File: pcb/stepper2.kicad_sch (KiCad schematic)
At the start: 52 parts, among them J1 DA15_Receptacle_MountingHoles, J10 Conn_01x07_Pin, J11 FAN, J2 DA15_Receptacle_MountingHoles, J3 DA15_Receptacle_MountingHoles, J4 DE15_Receptacle_HighDensity, J5 DE15_Receptacle_HighDensity, J6 DE15_Receptacle_HighDensity, J7 Conn_01x04_Pin, J8 Conn_01x05_Pin, J9 Conn_01x06_Pin, SW1 SW_Push, U1 AM26LS32ACN, U2 AM26LS32Ax, U3 AM26LS32ACN, U4 TMC2209_BIGTREETECH, U5 TMC2209_BIGTREETECH, U6 TMC2209_BIGTREETECH

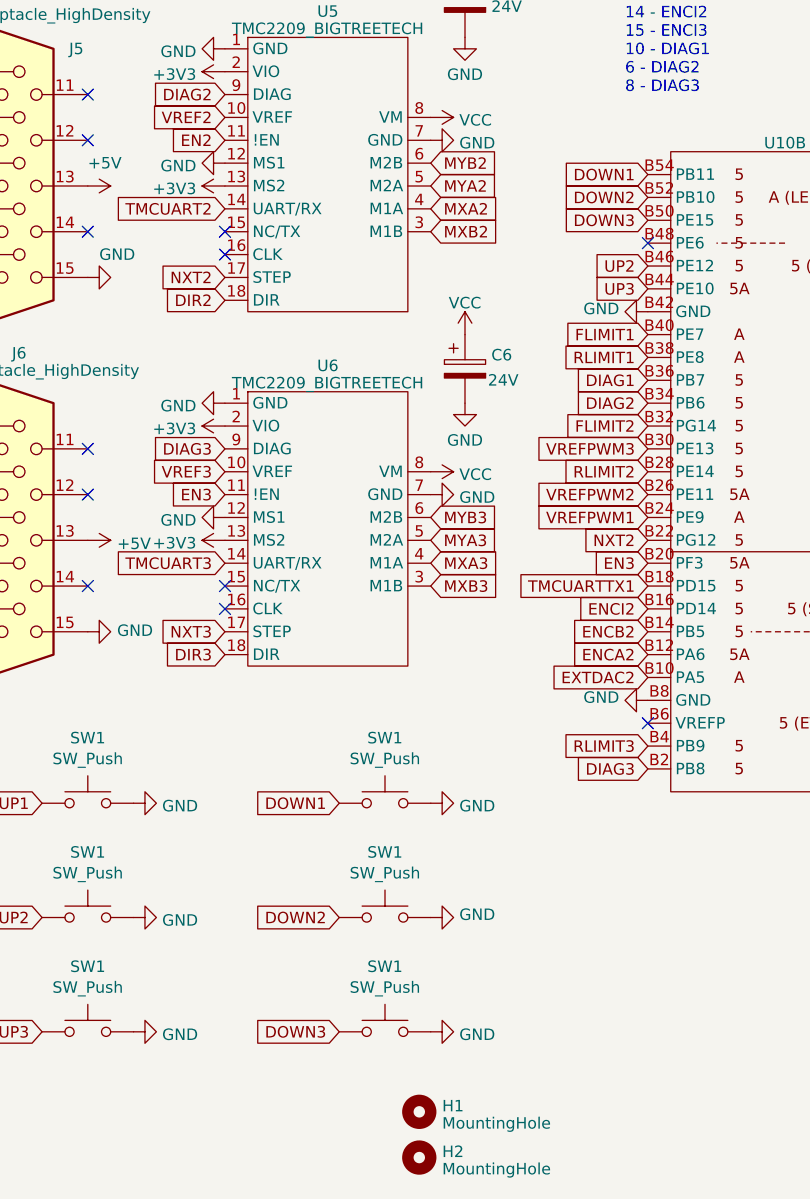
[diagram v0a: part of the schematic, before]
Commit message: fixed mixed labeling for jog buttons; initial config of the NXT timers
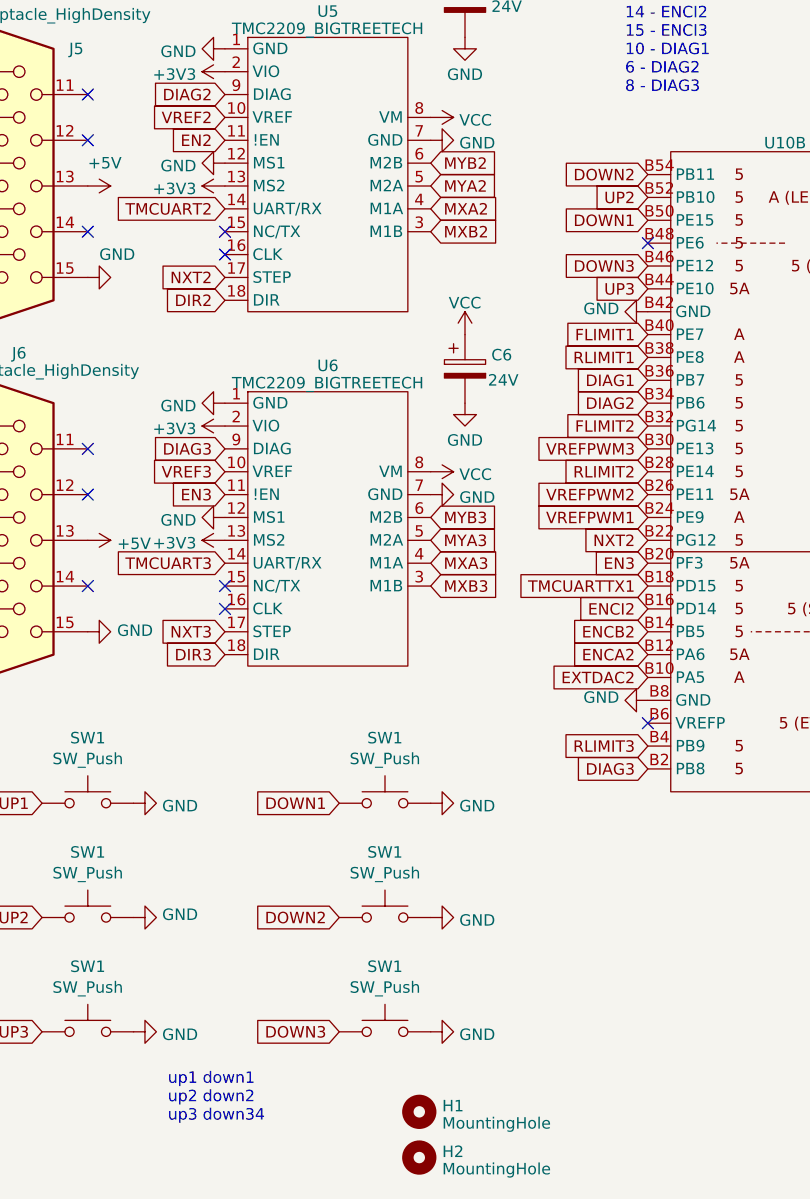
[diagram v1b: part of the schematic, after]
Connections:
- net DOWN1: now also SW1.1, U10.B50 (PE15); no longer SW1.1, U10.B54 (PB11)
- net DOWN2: now also SW1.1, U10.B54 (PB11); no longer SW1.1, U10.B52 (PB10)
- net DOWN3: now also SW1.1, U10.B46 (PE12); no longer SW1.1, U10.B50 (PE15)
- net UP2: now also SW1.1, U10.B52 (PB10); no longer SW1.1, U10.B46 (PE12)
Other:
- note added: "up1 down1 up2 down2 up3 down34"
- moved on the sheet: SW1

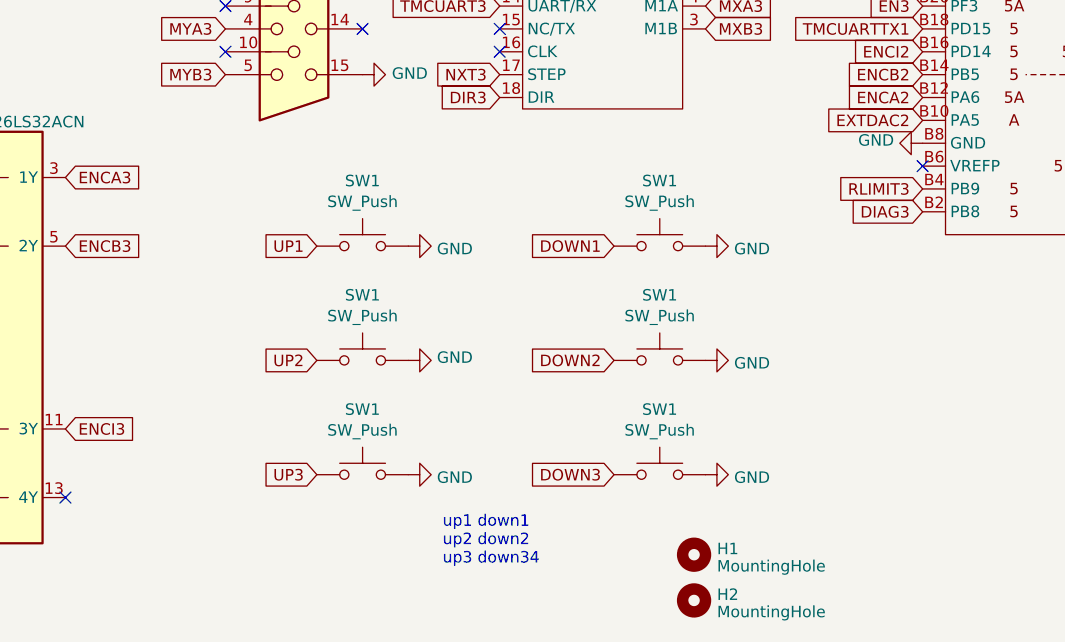
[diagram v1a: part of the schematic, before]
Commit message: PCB: NXT/DIR external output connectors and some polishing
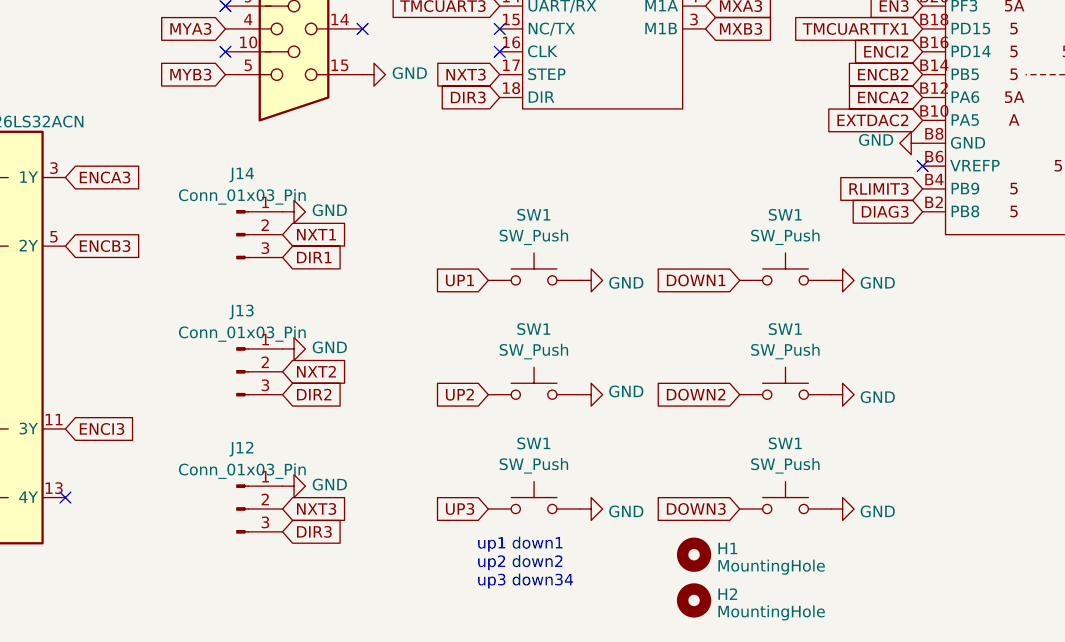
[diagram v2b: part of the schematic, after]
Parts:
- added J12, J13, J14: Conn_01x03_Pin, stepper2:JST_PH_S3B-PH-SM4-TB_1x03-1MP_P2.00mm_Horizontal, symbol Connector:Conn_01x03_Pin
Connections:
- net DIR1: now also J14.3 (Pin_3)
- net DIR2: now also J13.3 (Pin_3)
- net DIR3: now also J12.3 (Pin_3)
- net GND: now also J12.1 (Pin_1), J13.1 (Pin_1), J14.1 (Pin_1)
- net NXT1: now also J14.2 (Pin_2)
- net NXT2: now also J13.2 (Pin_2)
- net NXT3: now also J12.2 (Pin_2)
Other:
- moved on the sheet: SW1

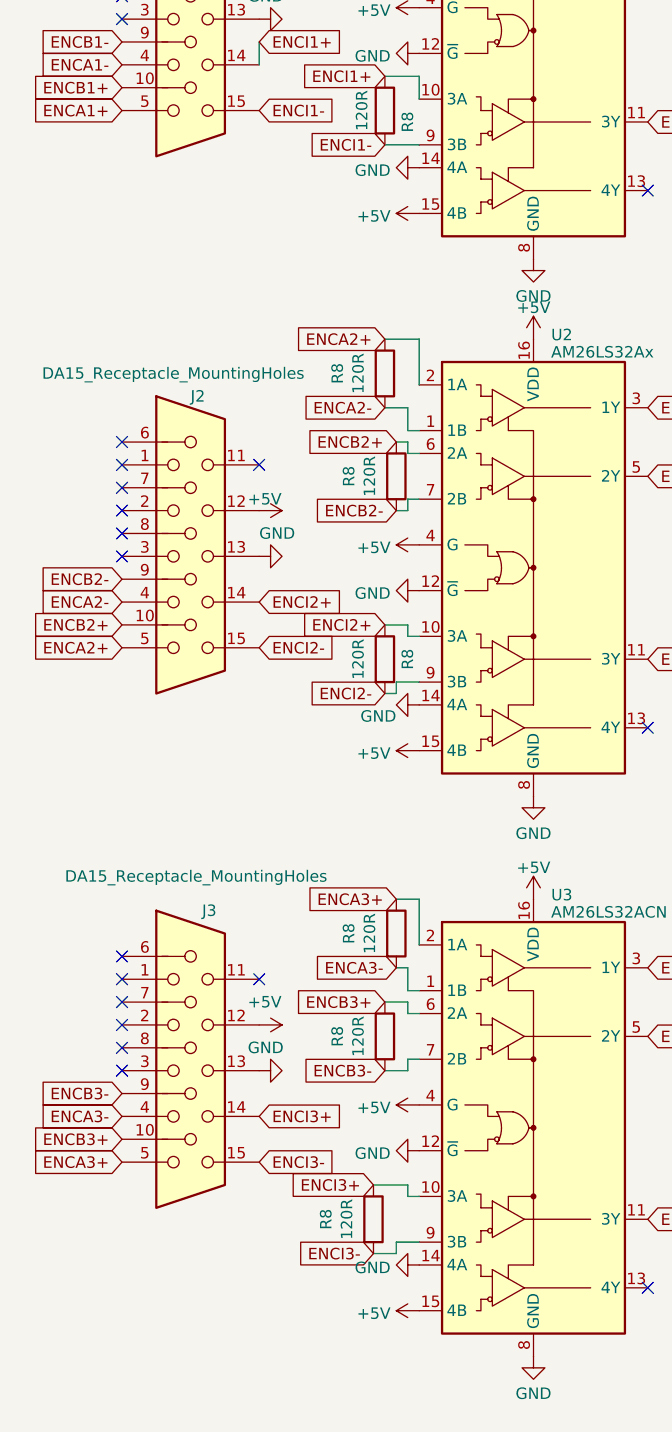
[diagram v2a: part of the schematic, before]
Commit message: filtering capacitors for differential receivers; BOM and placement files for SMD elements
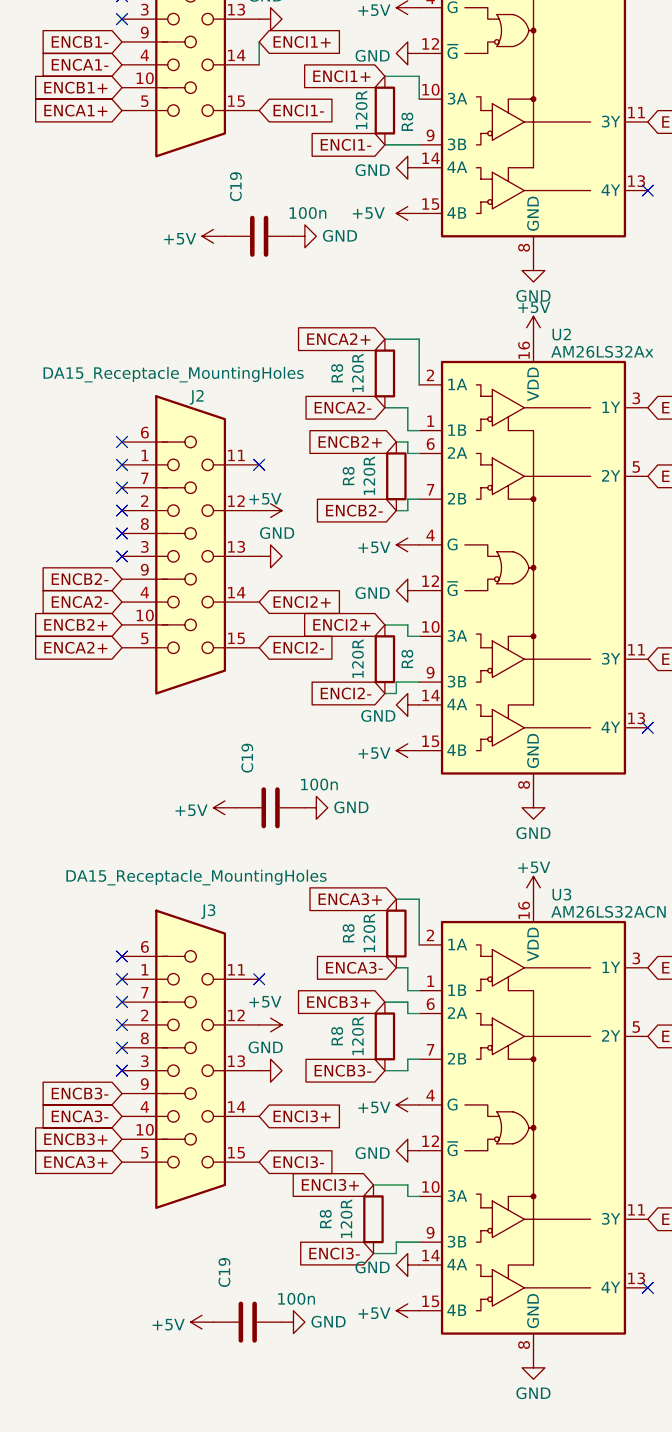
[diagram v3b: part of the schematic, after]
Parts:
- added C19 (x3): 100n, Capacitor_SMD:C_1206_3216Metric_Pad1.33x1.80mm_HandSolder, symbol Device:C
- C19: LCSC (none) -> C12891
- C4, C5, C6: LCSC (none) -> C2880403
- C7: LCSC (none) -> C310836
- J10: LCSC (none) -> C2856758
- J12, J13, J14: LCSC (none) -> C2688785
- J7: LCSC (none) -> C2688786
- J8: LCSC (none) -> C2874530
- J9: LCSC (none) -> C2874531
- R8: LCSC (none) -> C17909
- R8: LCSC (none) -> C17902
- R8: LCSC (none) -> C4410
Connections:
- net +5V: now also C19.1, C19.1, C19.1
- net GND: now also C19.2, C19.2, C19.2

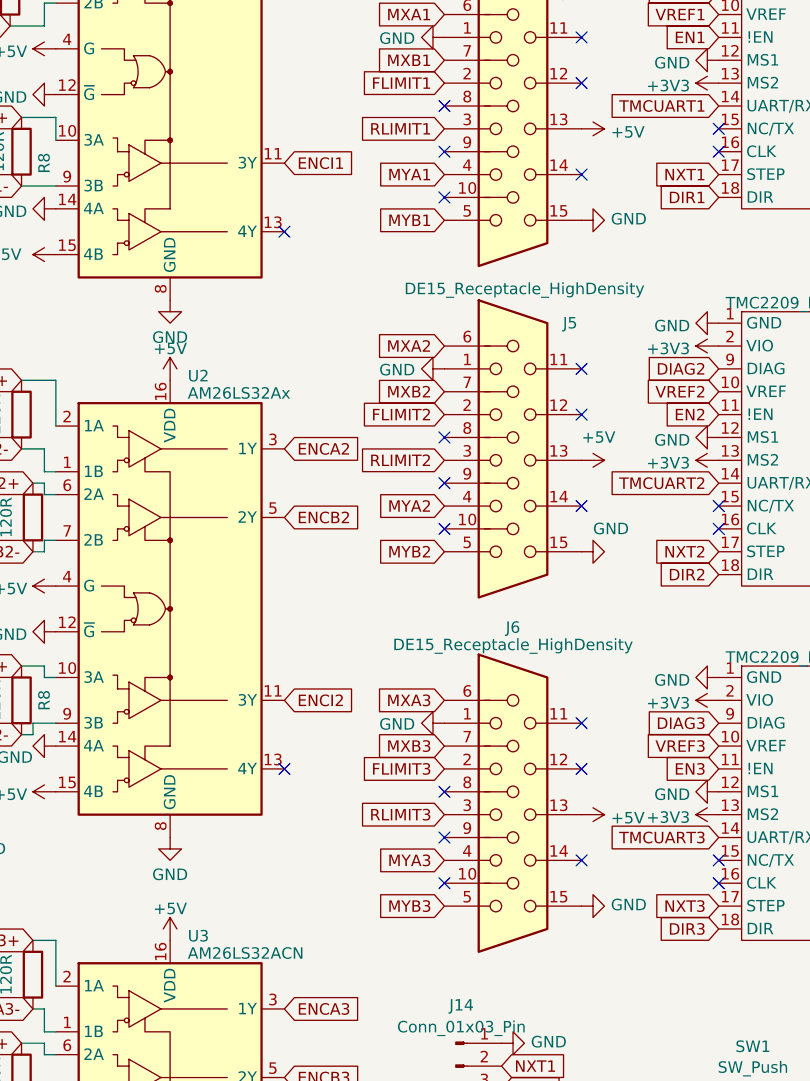
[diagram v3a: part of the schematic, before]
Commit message: fixed flipped rotation direction relative to stepper 1
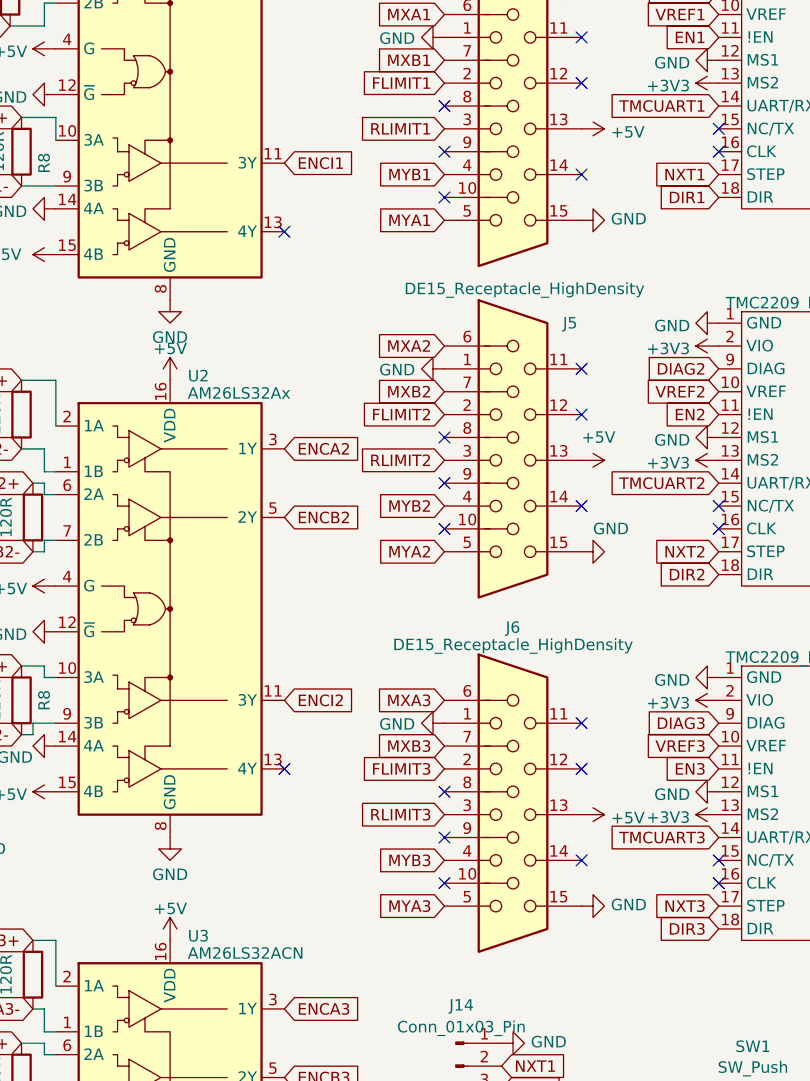
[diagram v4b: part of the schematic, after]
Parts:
- SW1: LCSC (none) -> C455126
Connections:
- net MYA1: now also J4.5; no longer J4.4
- net MYA2: now also J5.5; no longer J5.4
- net MYA3: now also J6.5; no longer J6.4
- net MYB1: now also J4.4; no longer J4.5
- net MYB2: now also J5.4; no longer J5.5
- net MYB3: now also J6.4; no longer J6.5
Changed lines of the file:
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@@
     )
   )
-  (global_label "MYB1" (shape input) (at 97.79 60.96 180) (fields_autoplaced)
+  (global_label "MYB1" (shape input) (at 97.79 55.88 180) (fields_autoplaced)
     (effects (font (size 1.27 1.27)) (justify right))
-    (property "Intersheetrefs" "${INTERSHEET_REFS}" (at 89.8647 60.96 0)
+    (property "Intersheetrefs" "${INTERSHEET_REFS}" (at 89.8647 55.88 0)
       (effects (font (size 1.27 1.27)) (justify right) hide)
     )
@@
     )
   )
-  (global_label "MYA1" (shape input) (at 97.79 55.88 180) (fields_autoplaced)
+  (global_label "MYA1" (shape input) (at 97.79 60.96 180) (fields_autoplaced)
     (effects (font (size 1.27 1.27)) (justify right))
-    (property "Intersheetrefs" "${INTERSHEET_REFS}" (at 90.0461 55.88 0)
+    (property "Intersheetrefs" "${INTERSHEET_REFS}" (at 90.0461 60.96 0)
       (effects (font (size 1.27 1.27)) (justify right) hide)
     )
@@
     )
   )
-  (global_label "MYA3" (shape input) (at 97.79 132.08 180) (fields_autoplaced)
+  (global_label "MYA3" (shape input) (at 97.79 137.16 180) (fields_autoplaced)
     (effects (font (size 1.27 1.27)) (justify right))
-    (property "Intersheetrefs" "${INTERSHEET_REFS}" (at 90.0461 132.08 0)
+    (property "Intersheetrefs" "${INTERSHEET_REFS}" (at 90.0461 137.16 0)
       (effects (font (size 1.27 1.27)) (justify right) hide)
     )
@@
     )
   )
-  (global_label "MYA2" (shape input) (at 97.79 92.71 180) (fields_autoplaced)
+  (global_label "MYA2" (shape input) (at 97.79 97.79 180) (fields_autoplaced)
     (effects (font (size 1.27 1.27)) (justify right))
-    (property "Intersheetrefs" "${INTERSHEET_REFS}" (at 90.0461 92.71 0)
+    (property "Intersheetrefs" "${INTERSHEET_REFS}" (at 90.0461 97.79 0)
       (effects (font (size 1.27 1.27)) (justify right) hide)
     )
@@
     )
   )
-  (global_label "MYB2" (shape input) (at 97.79 97.79 180) (fields_autoplaced)
+  (global_label "MYB2" (shape input) (at 97.79 92.71 180) (fields_autoplaced)
     (effects (font (size 1.27 1.27)) (justify right))
-    (property "Intersheetrefs" "${INTERSHEET_REFS}" (at 89.8647 97.79 0)
+    (property "Intersheetrefs" "${INTERSHEET_REFS}" (at 89.8647 92.71 0)
       (effects (font (size 1.27 1.27)) (justify right) hide)
     )
   )
-  (global_label "MYB3" (shape input) (at 97.79 137.16 180) (fields_autoplaced)
+  (global_label "MYB3" (shape input) (at 97.79 132.08 180) (fields_autoplaced)
     (effects (font (size 1.27 1.27)) (justify right))
-    (property "Intersheetrefs" "${INTERSHEET_REFS}" (at 89.8647 137.16 0)
+    (property "Intersheetrefs" "${INTERSHEET_REFS}" (at 89.8647 132.08 0)
       (effects (font (size 1.27 1.27)) (justify right) hide)
     )
@@
       (effects (font (size 1.27 1.27)) hide)
     )
+    (property "LCSC" "C455126" (at 160.02 185.42 0)
+      (effects (font (size 1.27 1.27)) hide)
+    )
     (pin "1")
     (pin "2")
@@
       (effects (font (size 1.27 1.27)) hide)
     )
+    (property "LCSC" "C455126" (at 160.02 160.02 0)
+      (effects (font (size 1.27 1.27)) hide)
+    )
     (pin "1")
     (pin "2")
@@
       (effects (font (size 1.27 1.27)) hide)
     )
+    (property "LCSC" "C455126" (at 160.02 172.72 0)
+      (effects (font (size 1.27 1.27)) hide)
+    )
     (pin "1")
     (pin "2")
@@
       (effects (font (size 1.27 1.27)) hide)
     )
+    (property "LCSC" "C455126" (at 132.08 185.42 0)
+      (effects (font (size 1.27 1.27)) hide)
+    )
     (pin "1")
     (pin "2")
@@
       (effects (font (size 1.27 1.27)) hide)
     )
+    (property "LCSC" "C455126" (at 132.08 160.02 0)
+      (effects (font (size 1.27 1.27)) hide)
+    )
     (pin "1")
     (pin "2")
@@
       (effects (font (size 1.27 1.27)) hide)
     )
+    (property "LCSC" "C455126" (at 132.08 172.72 0)
+      (effects (font (size 1.27 1.27)) hide)
+    )
